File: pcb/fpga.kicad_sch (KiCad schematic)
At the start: 20 parts, among them J13 KB, J5 FPGA JTAG, J7 RAM cacheable, J8 ROM cacheable, U2 XC2S100TQ144, Y1 TXC-7C, Y2 GTXO-14T

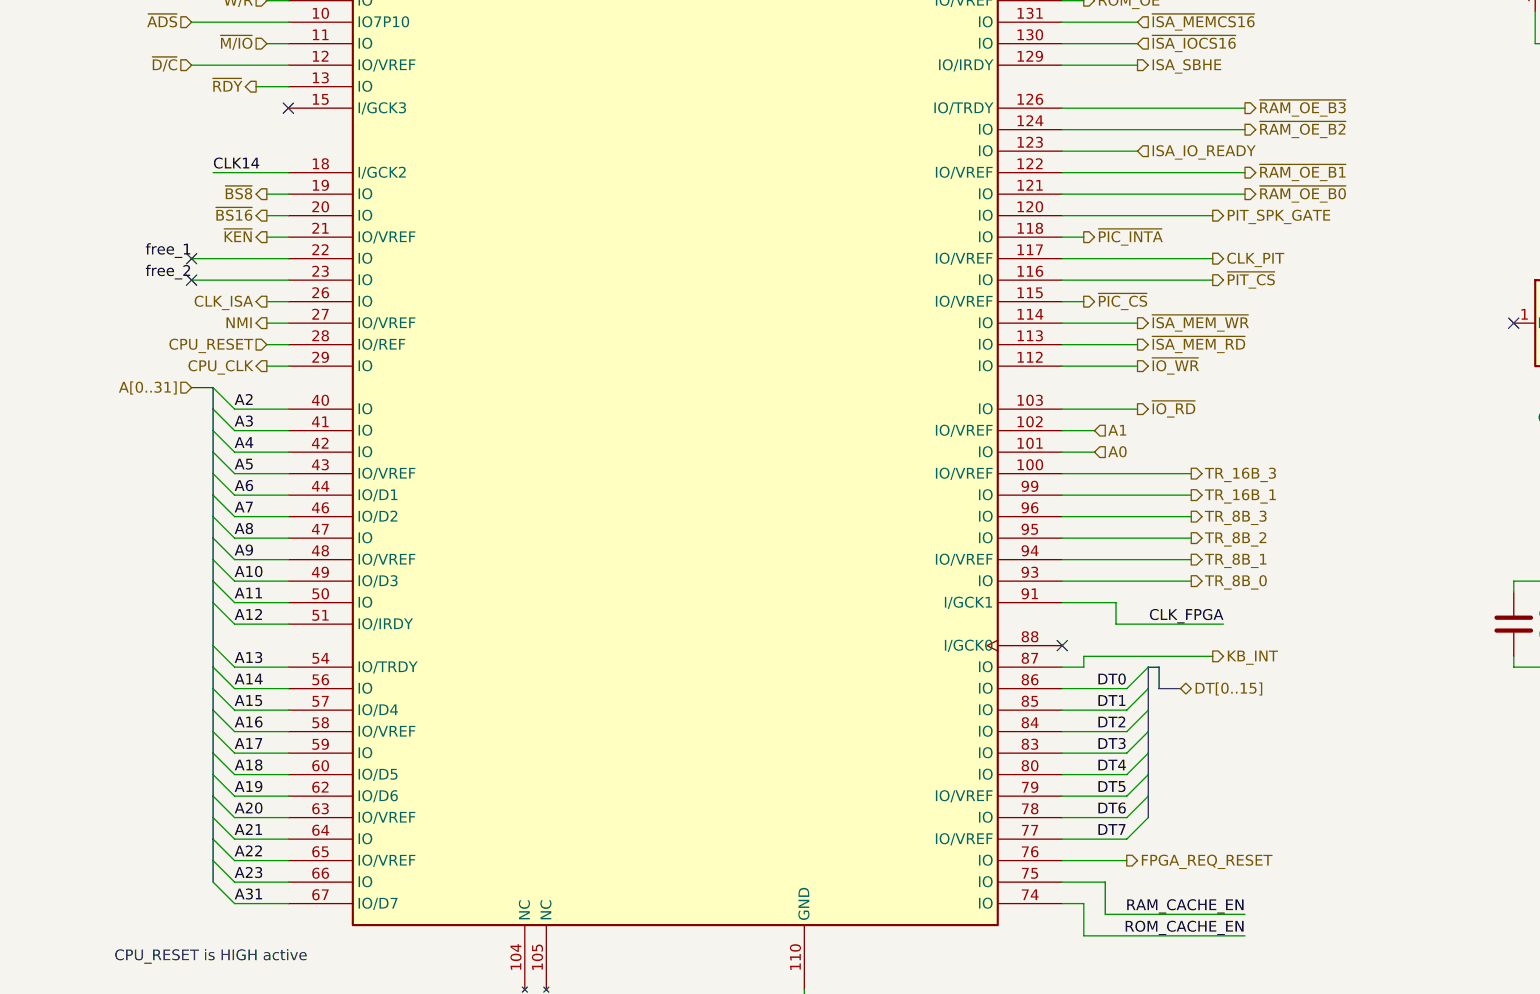
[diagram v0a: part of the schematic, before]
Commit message: moved CLK14 CLK_IN_14_318 pin 12->88, making room near critical FPGA-CPU pins
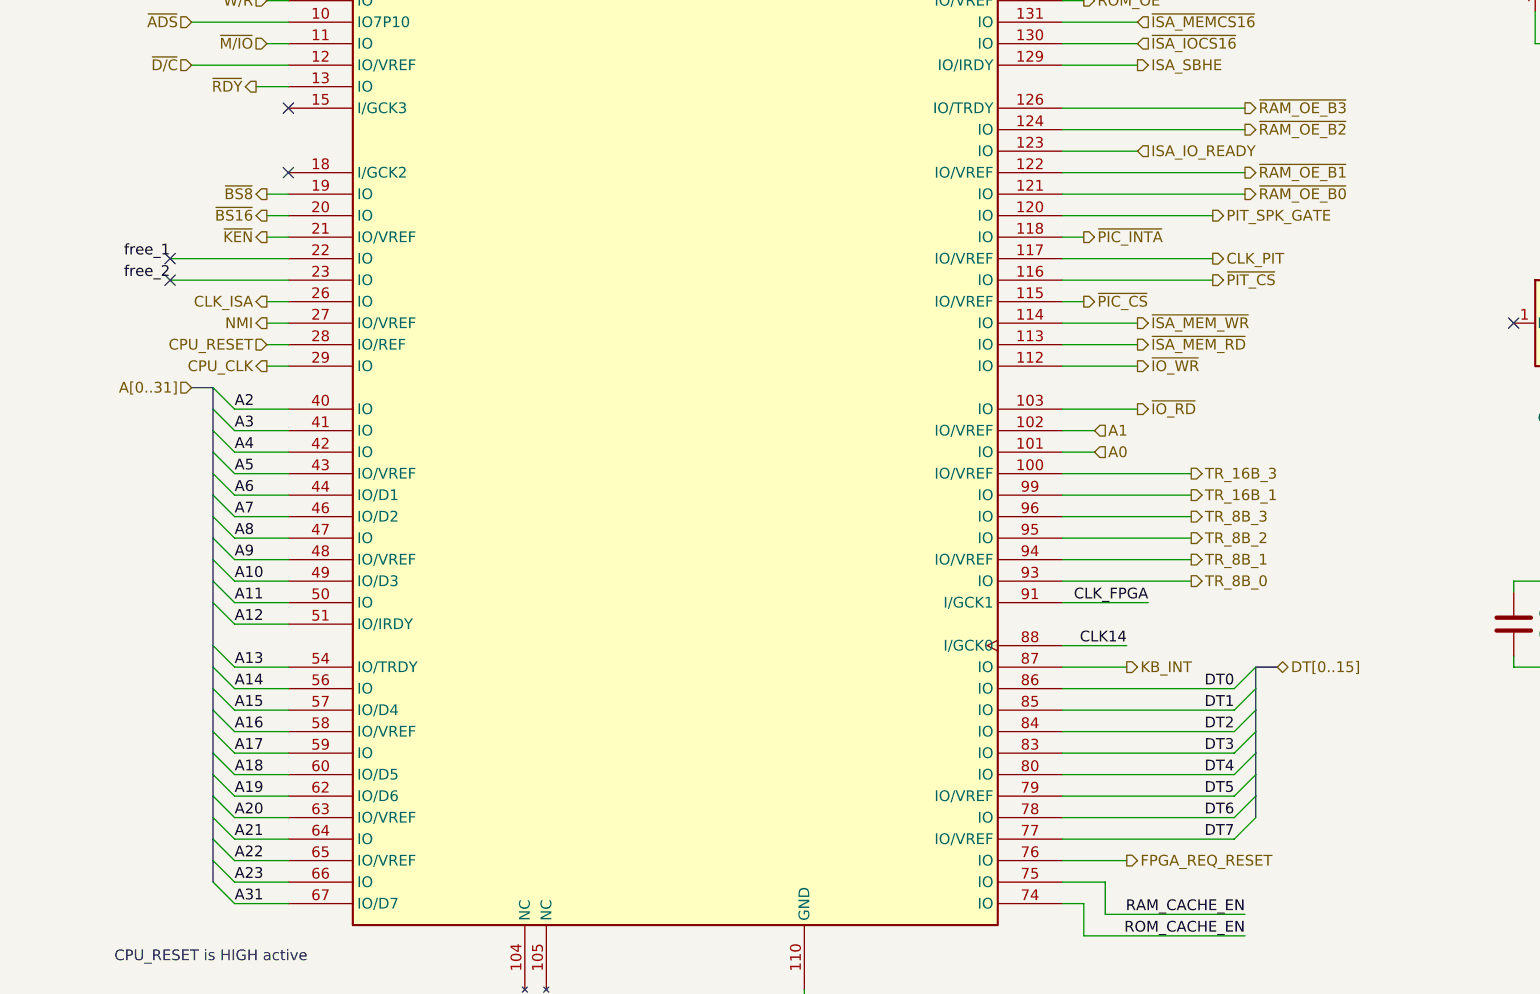
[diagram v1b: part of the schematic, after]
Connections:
- net CLK_14_318MHz: now also U2.88 (I/GCK0); no longer U2.18 (I/GCK2)
